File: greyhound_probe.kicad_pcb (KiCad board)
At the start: 2 copper layers, 40 parts, among them J1 USB_C_Receptacle_USB2.0, J2 Conn_01x04_Male, J3 FTSH-105-01-L-DV-K-TR, Q1 IRLML6401, SW1 SW_SPDT, U1 XC6206P332MR, U2 USBLC6-2SC6, U3 STM32F072CBUx

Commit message: Fixed short and power symbols
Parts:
- moved R11 5.17 mm to (148.6, 77.5), turned to 180 degrees
- moved R8 3.30 mm to (137.7, 71.8)
- moved J2 3.03 mm to (136.8, 87.5)
- moved J3 2.80 mm to (154.5, 79.8), turned to 180 degrees
- moved H3 2.45 mm to (155.4, 70.5)
- moved RN1 2.36 mm to (148.6, 80.0), turned to 180 degrees
- moved H4 2.35 mm to (122.7, 68.8)
- moved H2 2.31 mm to (155.4, 87.5)
- moved H1 2.25 mm to (122.9, 87.4)
- moved R10 2.05 mm to (142.2, 84.2)
- moved R9 2.05 mm to (140.8, 84.2)
- moved R2 1.55 mm to (128.2, 74.8)
- moved C5 1.12 mm to (144.9, 83.8)
- moved C4 1.12 mm to (146.4, 83.8)
- moved R1 0.92 mm to (128.2, 81.3)
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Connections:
- C1 pad 2: +3.3V -> GND
- C10 pad 2: +3.3V -> GND
- C11 pad 2: +3.3V -> GND
- C2 pad 2: +3.3V -> GND
- C3 pad 2: +3.3V -> GND
- C4 pad 2: +3.3V -> GND
- C5 pad 2: +3.3V -> GND
- C6 pad 2: +3.3V -> GND
- C7 pad 2: +3.3V -> GND
- C8 pad 2: +3.3V -> GND
- C9 pad 2: +3.3V -> GND
- D1 pad 1: +3.3V -> GND
- D2 pad 1: +3.3V -> GND
- D3 pad 1: +3.3V -> GND
- J1 pad A1: +3.3V -> GND
- J1 pad A12: +3.3V -> GND
- J1 pad B1: +3.3V -> GND
- J1 pad B12: +3.3V -> GND
- J2 pad 4: +3.3V -> GND
- J3 pad 3: +3.3V -> GND
- J3 pad 5: +3.3V -> GND
- J3 pad 9: +3.3V -> GND
- R1 pad 1: +3.3V -> GND
- R2 pad 1: +3.3V -> GND
- R4 pad 2: +3.3V -> GND
- SW1 pad 1: +3.3V -> GND
- U1 pad 1: +3.3V -> GND
- U2 pad 2: +3.3V -> GND
- U3 pad 23: +3.3V -> GND
- U3 pad 25: /TARGET_TDO -> /TARGET_TCK
- U3 pad 26: /TARGET_TCK -> /TARGET_TMS
- U3 pad 27: /TARGET_TMS -> /TARGET_TDO
- U3 pad 35: +3.3V -> GND
- U3 pad 47: +3.3V -> GND
- U3 pad 49: +3.3V -> GND
- U3 pad 8: +3.3V -> GND

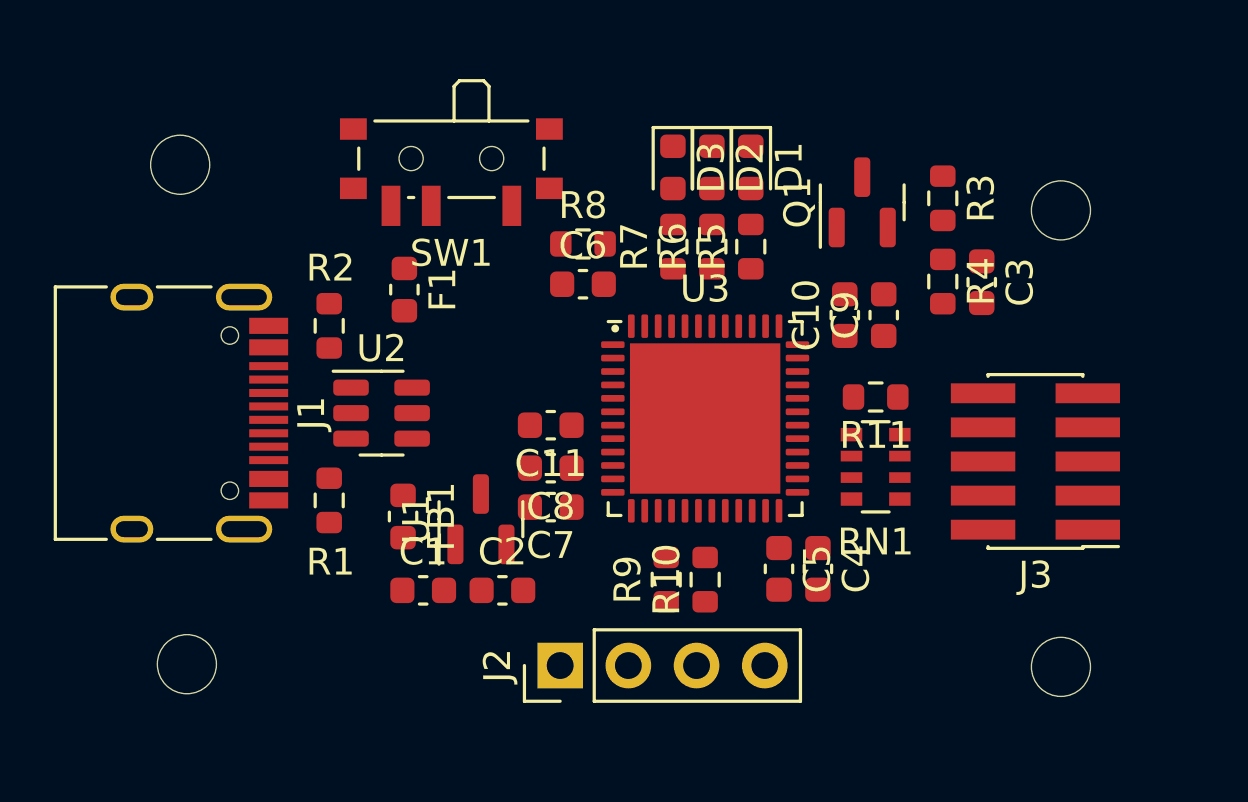
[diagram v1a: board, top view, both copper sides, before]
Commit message: PCB positioning changes, silkscreen changes
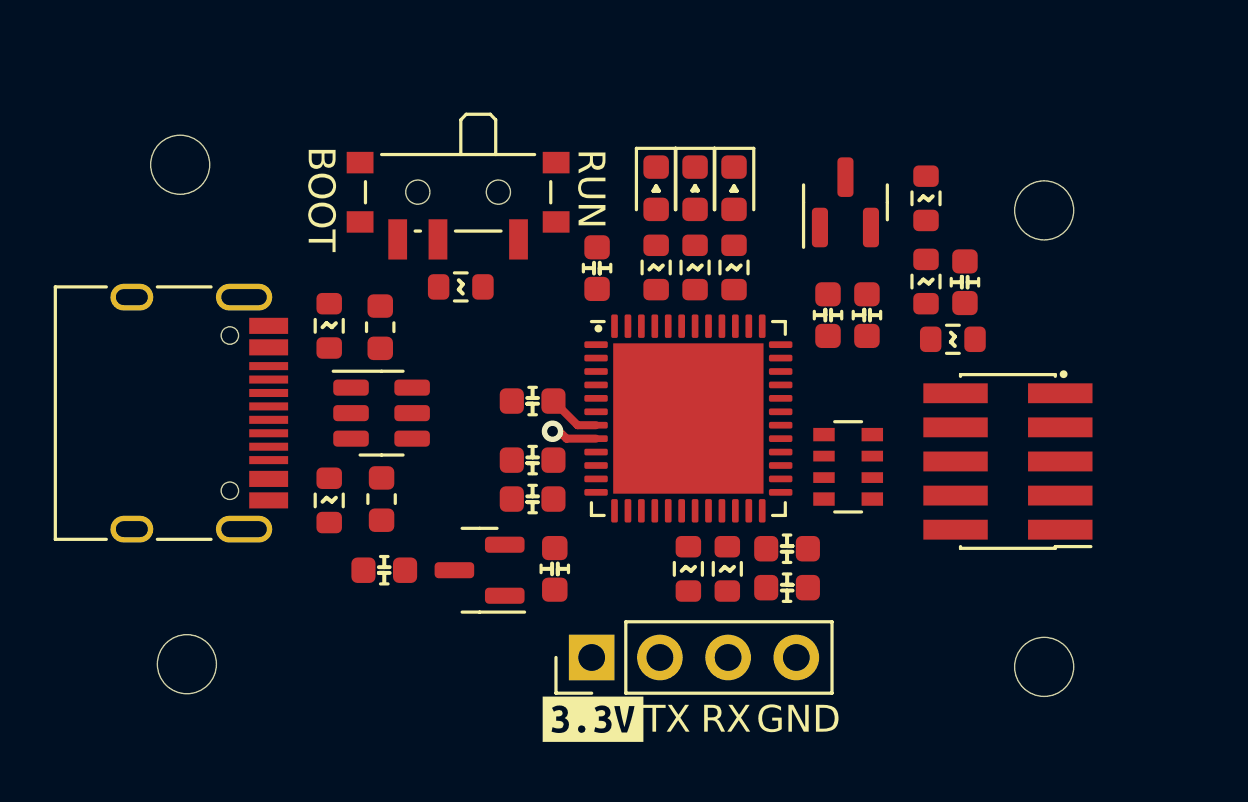
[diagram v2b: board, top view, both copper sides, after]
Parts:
- added kibuzzard-6311E48F: G***, kibuzzard-6311E48F, F.Cu at (138.0, 89.5)
- moved R8 4.82 mm to (133.1, 73.3)
- moved R11 3.59 mm to (151.4, 75.3)
- moved C2 2.11 mm to (136.6, 83.8), turned to -90 degrees
- moved U1 1.90 mm to (133.8, 83.9), turned to 180 degrees
- moved F1 1.66 mm to (130.1, 74.8)
- moved C1 1.63 mm to (130.2, 83.9), turned to 180 degrees
- moved C4 1.35 mm to (145.2, 84.5), turned to 0 degrees
- moved SW1 1.27 mm to (133.0, 70.2)
- moved J2 1.21 mm to (138.0, 87.2)
- moved C11 1.12 mm to (135.8, 77.6)
- moved FB1 1.03 mm to (130.2, 81.2)
- moved J3 1.03 mm to (153.5, 79.8)
- moved RN1 1.03 mm to (147.5, 80.0)
- moved R5 1.00 mm to (143.3, 72.6)
- moved R6 1.00 mm to (141.8, 72.6)
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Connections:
- RN1 pad 1: Net-(J3-Pad4) -> Net-(J3-Pad2)
- RN1 pad 2: Net-(J3-Pad2) -> Net-(J3-Pad4)
- RN1 pad 7: /TARGET_TMS -> /TARGET_TCK
- RN1 pad 8: /TARGET_TCK -> /TARGET_TMS
- U3 pad 25: /TARGET_TCK -> /TARGET_TMS
- U3 pad 26: /TARGET_TMS -> /TARGET_TCK
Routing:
- net /NRST: track 0.00 -> 1.96 mm
- net GND: track 0.00 -> 1.73 mm, vias 0 -> 1
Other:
- copper layers 2 -> 4
- board text added: "BOOT"
- board text added: "GND"
- board text added: "RUN"
- board text added: "RX"
- board text added: "TX"

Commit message: Routing mostly done, rough board outline
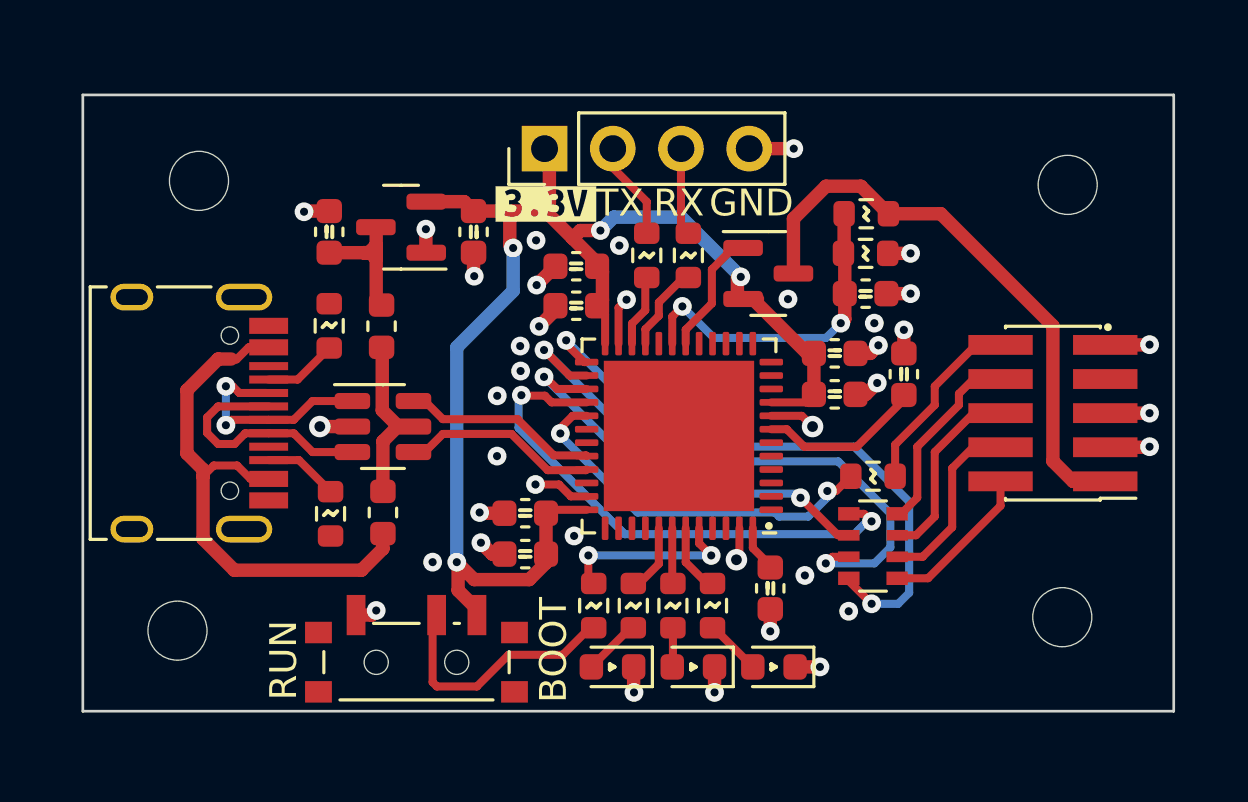
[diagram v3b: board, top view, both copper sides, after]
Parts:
- moved kibuzzard-6311E48F 19.3 mm to (136.3, 70.2)
- moved J2 19.0 mm to (136.2, 68.2)
- moved D1 18.4 mm to (138.8, 87.5), turned to 180 degrees
- moved D3 18.4 mm to (144.8, 87.5), turned to 180 degrees
- moved D2 17.8 mm to (141.8, 87.5), turned to 180 degrees
- moved SW1 16.9 mm to (131.4, 87.0), turned to 0 degrees
- moved C9 15.5 mm to (135.5, 83.3), turned to 180 degrees
- moved C4 14.3 mm to (137.4, 72.6), turned to 180 degrees
- moved C11 13.9 mm to (149.6, 76.6), turned to 90 degrees
- moved C6 13.6 mm to (144.6, 84.6), turned to -90 degrees
- moved C10 13.5 mm to (135.5, 81.8), turned to 180 degrees
- moved R5 13.1 mm to (139.5, 85.2), turned to -90 degrees
- moved U1 13.1 mm to (130.9, 71.1)
- moved C2 12.9 mm to (133.6, 71.3)
- moved R8 12.9 mm to (138.1, 85.2), turned to 90 degrees
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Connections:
- R10 pad 2: /UART_RX -> /UART_TX
- R9 pad 2: /UART_TX -> /UART_RX
- U2 pad 1: /USB_CONN_D+ -> /USB_CONN_D-
- U2 pad 3: /USB_CONN_D- -> /USB_CONN_D+
- U2 pad 4: /USB_D- -> /USB_D+
- U2 pad 6: /USB_D+ -> /USB_D-
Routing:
- net +3.3V: track 0.00 -> 54.6 mm, vias 0 -> 4
- net GND: track 1.73 -> 30.4 mm, vias 1 -> 38
- net /TARGET_TMS: track 0.00 -> 22.7 mm, vias 0 -> 2
- net /TARGET_TCK: track 0.00 -> 22.3 mm, vias 0 -> 2
- net /TARGET_VOLTAGE_RAW: track 0.00 -> 21.7 mm
- net /USB_FUSE: track 0.00 -> 20.4 mm
- net /TARGET_TDI: track 0.00 -> 19.8 mm, vias 0 -> 2
- net /TARGET_TDO: track 0.00 -> 15.6 mm, vias 0 -> 2
- net /TARGET_RST: track 0.00 -> 14.3 mm, vias 0 -> 2
- net /TARGET_VOLTAGE: track 0.00 -> 12.3 mm, vias 0 -> 2
- net Net-(R8-Pad1): track 0.00 -> 9.53 mm
- net /USB_CONN_D+: track 0.00 -> 9.08 mm
- net /USB_CONN_D-: track 0.00 -> 8.14 mm, vias 0 -> 2
- net Net-(J3-Pad8): track 0.00 -> 7.29 mm
- net /USB_D-: track 0.07 -> 7.30 mm
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- added copper zone on In1.Cu, net GND
- added copper zone on In2.Cu, net GND
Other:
- board outline added: 40.6 x 23 mm

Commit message: Routed the rest of pins, rounded corners, mounting holes placing
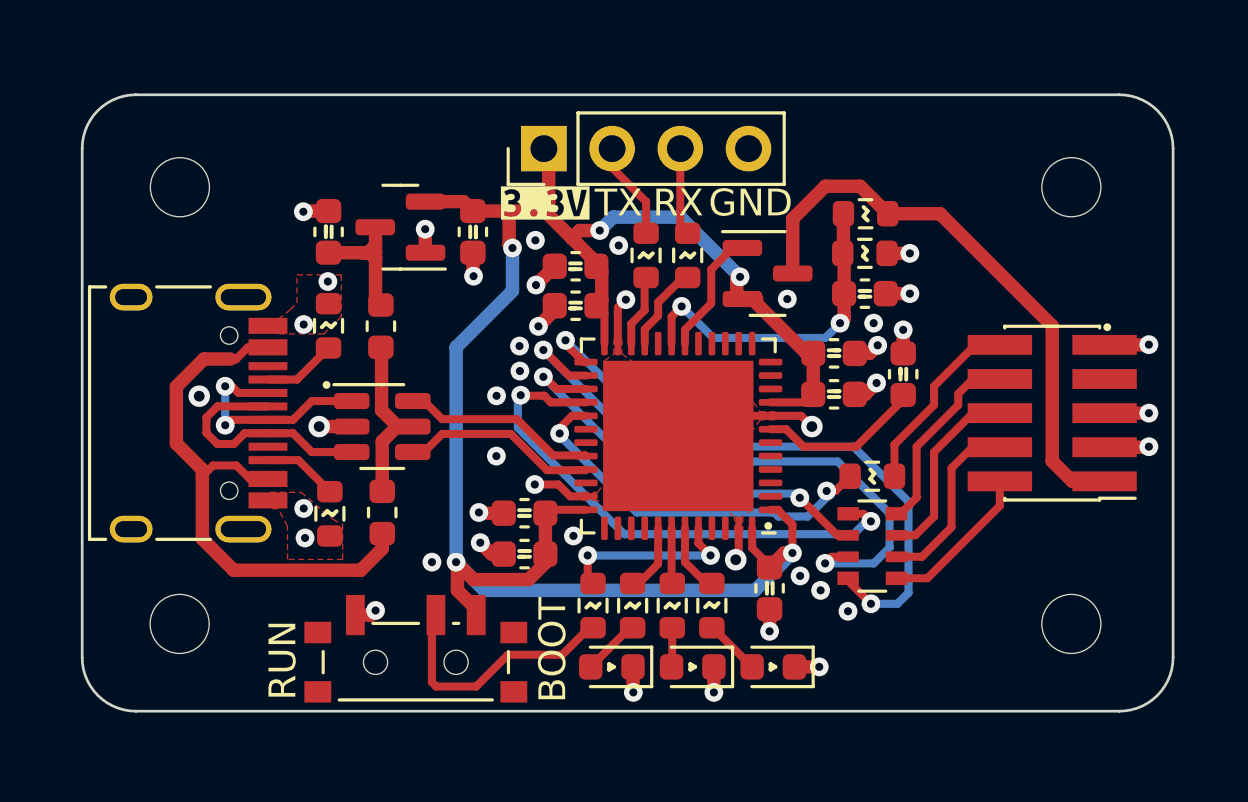
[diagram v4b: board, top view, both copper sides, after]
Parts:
- removed kibuzzard-6311E48F: G***, kibuzzard-6311E48F
- added kibuzzard-63127F62: G***, kibuzzard-63127F62, F.Cu at (136.2, 70.2)
- moved H4 0.75 mm to (122.6, 69.6)
- moved H2 0.42 mm to (155.8, 85.9)
- moved H1 0.26 mm to (122.6, 85.9)
- moved H3 0.16 mm to (155.8, 69.6)
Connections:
- J1 pad S1: unconnected-(J1-PadS1) -> (no net)
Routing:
- net +3.3V: track 54.6 -> 71.3 mm, vias 4 -> 5
- net GND: track 30.4 -> 32.5 mm, vias 38 -> 43
- net /USB_FUSE: track 20.4 -> 21.0 mm
- added copper zone on F.Cu, net GND
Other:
- outline, holes or cut-outs redrawn

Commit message: Added silkscreen labels
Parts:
- added G***: LOGO, LOGO, B.Cu at (151.8, 77.8)
- added kibuzzard-63139EF8: G***, kibuzzard-63139EF8, B.Cu at (155.8, 77.8)
- added kibuzzard-6313B2B7: G***, kibuzzard-6313B2B7, B.Cu at (157.6, 77.8)

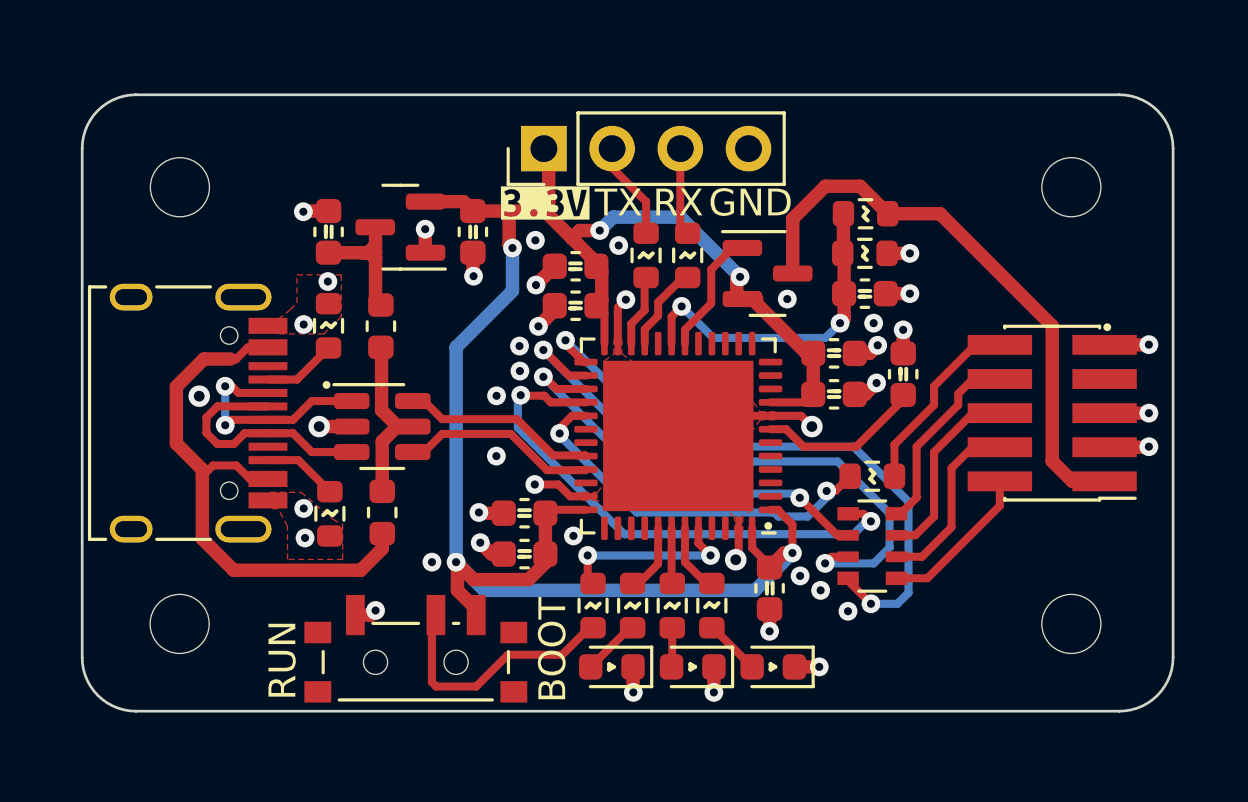
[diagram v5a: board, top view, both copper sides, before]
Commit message: Via stitching done
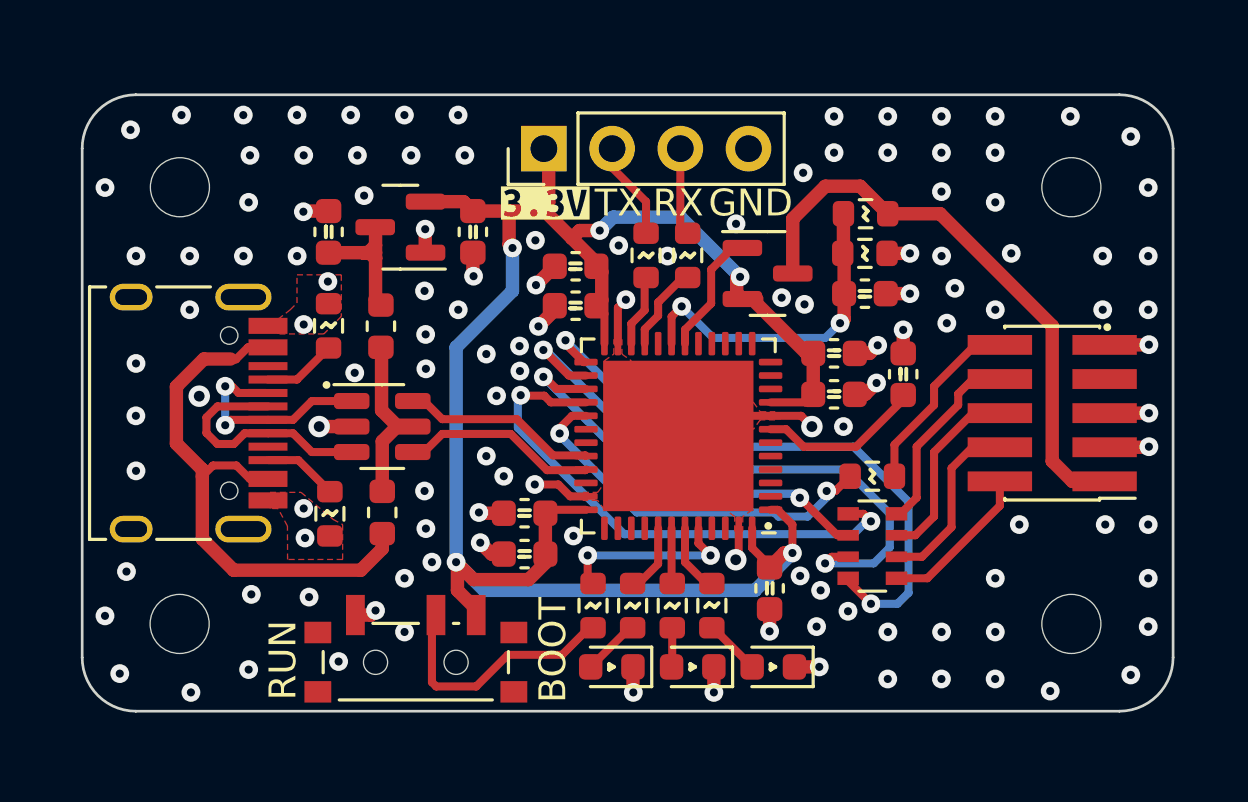
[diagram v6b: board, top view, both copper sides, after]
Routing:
- net GND: vias 43 -> 126
